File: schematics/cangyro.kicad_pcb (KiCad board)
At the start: 2 copper layers, 14 parts, among them J1 Conn_01x06 CAN & PWR, J2 Conn_01x10 IMU BNO080, P1 USB_C_Plug_USB2.0 Serial, SW1 SW_Push IMU_RST, U1 STM32G474CBTx, U2 MCP2562-E-MF, U3 AP2112K-3.3

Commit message: Switched MicroController To PiPco
- Base software with BNO08x lib and pico stuff
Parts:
- added J3: Conn_01x05 SYS, TerminalBlock_Phoenix:TerminalBlock_Phoenix_MKDS-1,5-6_1x06_P5.00mm_Horizontal, F.Cu at (138.0, 98.1)
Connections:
- U1 pad 37: unconnected-(U1-PA13-Pad37) -> /SWDIO
- U1 pad 38: unconnected-(U1-PA14-Pad38) -> /SWCLK
- U1 pad 39: unconnected-(U1-PA15-Pad39) -> /IMU_SCL
- U1 pad 43: /IMU_SCL -> unconnected-(U1-PB6-Pad43)
- U1 pad 7: unconnected-(U1-PG10-Pad7) -> /NRST

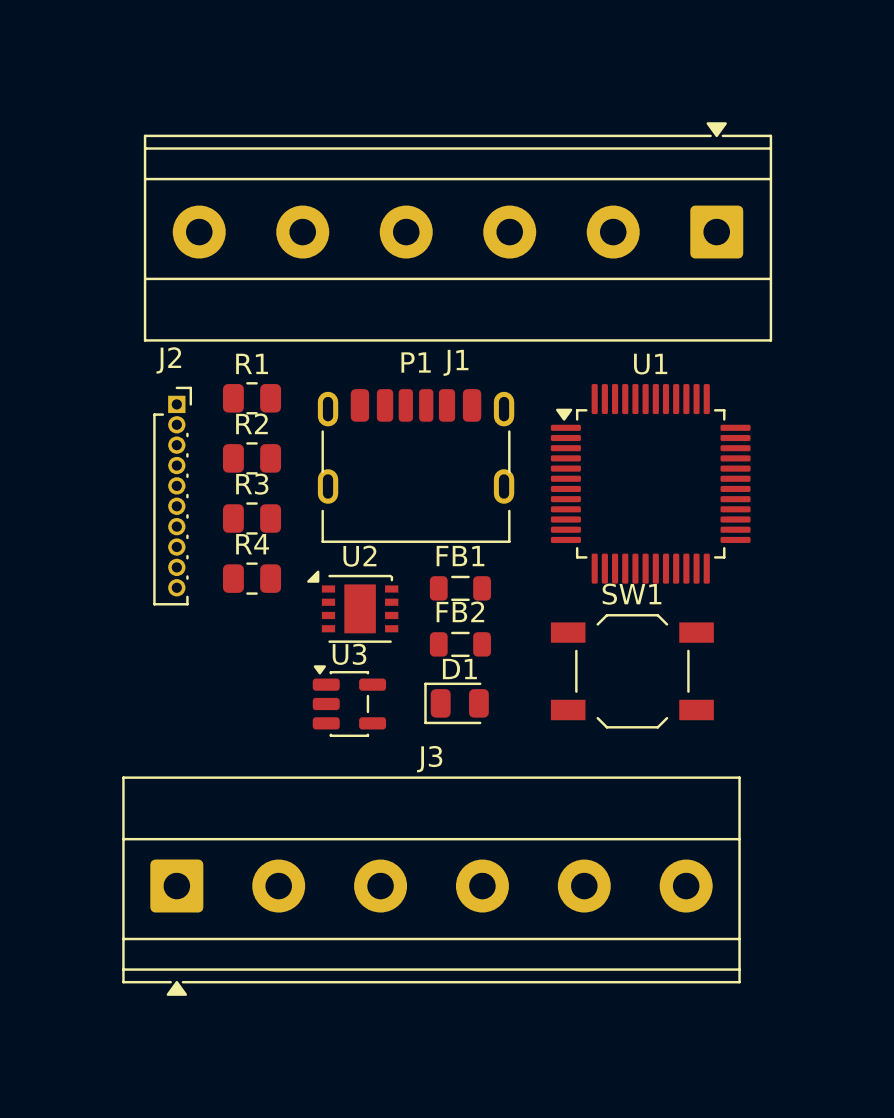
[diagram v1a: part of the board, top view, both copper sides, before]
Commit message: Added Footprints
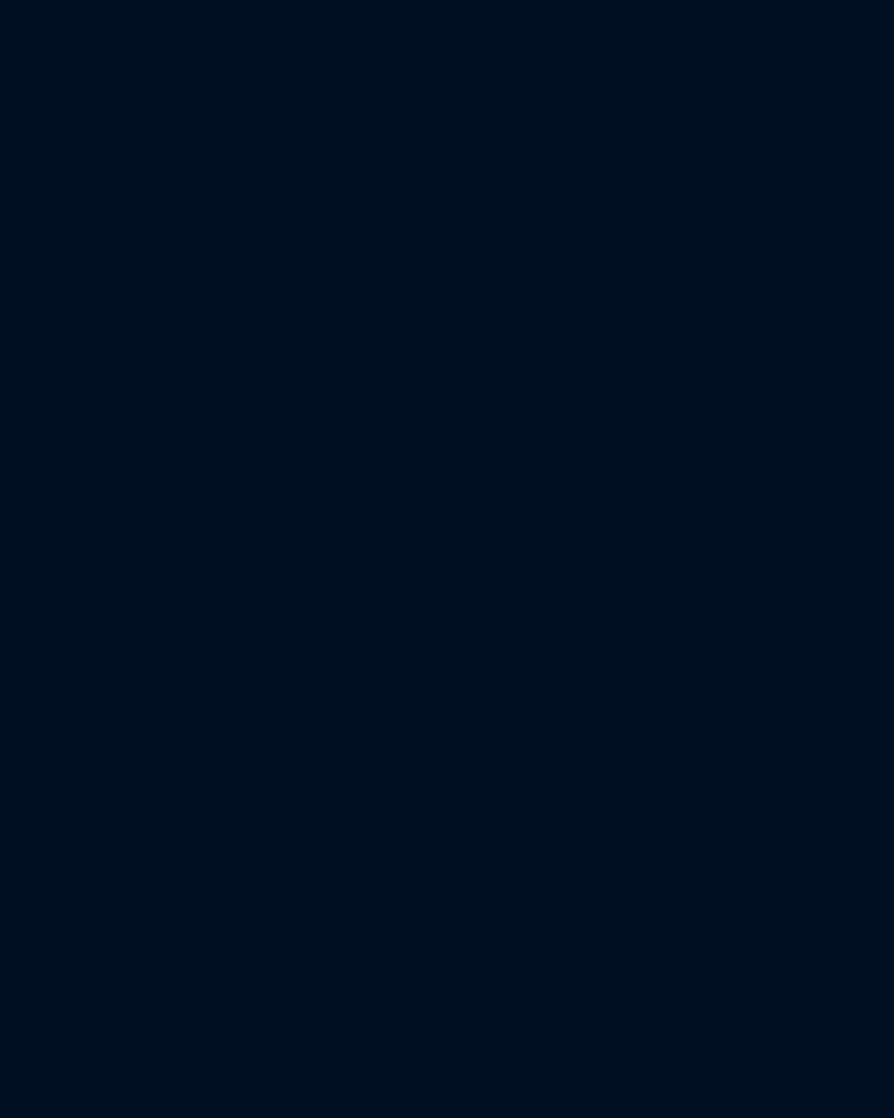
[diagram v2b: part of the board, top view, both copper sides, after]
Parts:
- removed D1: LED, LED_SMD:LED_0805_2012Metric
- removed FB1, FB2: FerriteBead, Inductor_SMD:L_0805_2012Metric
- removed J1: Conn_01x06 CAN & PWR, TerminalBlock_Phoenix:TerminalBlock_Phoenix_MKDS-1,5-6-5.08_1x06_P5.08mm_Horizontal
- removed J2: Conn_01x10 IMU BNO080, Connector_PinSocket_1.00mm:PinSocket_1x10_P1.00mm_Vertical
- removed J3: Conn_01x05 SYS, TerminalBlock_Phoenix:TerminalBlock_Phoenix_MKDS-1,5-6_1x06_P5.00mm_Horizontal
- removed P1: USB_C_Plug_USB2.0 Serial, Connector_USB:USB_C_Receptacle_HRO_TYPE-C-31-M-17
- removed R1: 1k, Resistor_SMD:R_0805_2012Metric
- removed R2, R3: 22Ohm, Resistor_SMD:R_0805_2012Metric
- removed R4: 5.1k Ohm, Resistor_SMD:R_0805_2012Metric
- removed SW1: SW_Push IMU_RST, Button_Switch_SMD:SW_SPST_TL3342
- removed U1: STM32G474CBTx, Package_QFP:LQFP-48_7x7mm_P0.5mm
- removed U2: MCP2562-E-MF, Package_DFN_QFN:DFN-8-1EP_3x3mm_P0.65mm_EP1.55x2.4mm
- removed U3: AP2112K-3.3, Package_TO_SOT_SMD:SOT-23-5

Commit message: Routing PCB with FreeRouting
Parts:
- added A1: RaspberryPi_Pico, Module:RaspberryPi_Pico_SMD_HandSolder, F.Cu at (120.9, 76.6)
- added C4: 4.7nF, Capacitor_SMD:C_0603_1608Metric, F.Cu at (135.7, 73.7)
- added C5: C, Capacitor_SMD:C_0603_1608Metric, F.Cu at (142.6, 73.8)
- added C6: C, Capacitor_SMD:C_0603_1608Metric, F.Cu at (139.2, 73.7)
- added D1: LED, LED_SMD:LED_0603_1608Metric, F.Cu at (137.2, 58.8)
- added J2: Conn_01x06, TerminalBlock_Phoenix:TerminalBlock_Phoenix_MKDS-1,5-6_1x06_P5.00mm_Horizontal, F.Cu at (154.8, 78.2)
- added J3: Conn_01x10 IMU BNO080, Connector_PinSocket_1.00mm:PinSocket_1x10_P1.00mm_Vertical, F.Cu at (158.6, 90.7)
- added R2: 10k, Resistor_SMD:R_0603_1608Metric, F.Cu at (142.8, 71.3)
- added R3: 300 Ohm, Resistor_SMD:R_0603_1608Metric, F.Cu at (135.8, 71.1)
- added R4: 10k, Resistor_SMD:R_0603_1608Metric, F.Cu at (139.4, 71.3)
- added SW1: SW_Push, Button_Switch_SMD:SW_Push_1P1T_NO_CK_KMR2, F.Cu at (157.2, 83.8)
- added U1: MCP2562-E-MF, Package_DFN_QFN:DFN-8-1EP_3x3mm_P0.65mm_EP1.55x2.4mm, F.Cu at (145.2, 81.2)
- added U4: MCP2515-xSO, Package_SO:SOIC-18W_7.5x11.6mm_P1.27mm, F.Cu at (143.1, 95.3)
- added Y2: Crystal, Crystal:Crystal_HC49-U-3Pin_Vertical, F.Cu at (138.4, 53.4)
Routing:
- net GND: track 0.00 -> 268.6 mm
- net 3V3: track 0.00 -> 90.9 mm, vias 0 -> 1
- net 5V: track 0.00 -> 72.6 mm, vias 0 -> 2
- net /CANBus Module/SO: track 0.00 -> 58.3 mm, vias 0 -> 2
- net /CANBus Module/SI: track 0.00 -> 54.9 mm, vias 0 -> 2
- net /CANBus Module/CS: track 0.00 -> 54.4 mm, vias 0 -> 2
- net Net-(U4-OSC1): track 0.00 -> 50.8 mm
- net Net-(U4-OSC2): track 0.00 -> 49.3 mm
- net /CANBus Module/SCK: track 0.00 -> 48.4 mm, vias 0 -> 2
- net Net-(A1-RUN): track 0.00 -> 43.4 mm, vias 0 -> 3
- net /CANBus Module/INT: track 0.00 -> 39.9 mm
- net /BNO080 Connector/SCL: track 0.00 -> 38.5 mm, vias 0 -> 1
- net /BNO080 Connector/RST: track 0.00 -> 32.0 mm, vias 0 -> 1
- net /BNO080 Connector/INT: track 0.00 -> 30.9 mm, vias 0 -> 1
- net /BNO080 Connector/SDA: track 0.00 -> 30.4 mm, vias 0 -> 1
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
